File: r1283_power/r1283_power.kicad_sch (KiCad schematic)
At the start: 23 parts, among them J6 Output, J7 Input, U1 R1283K

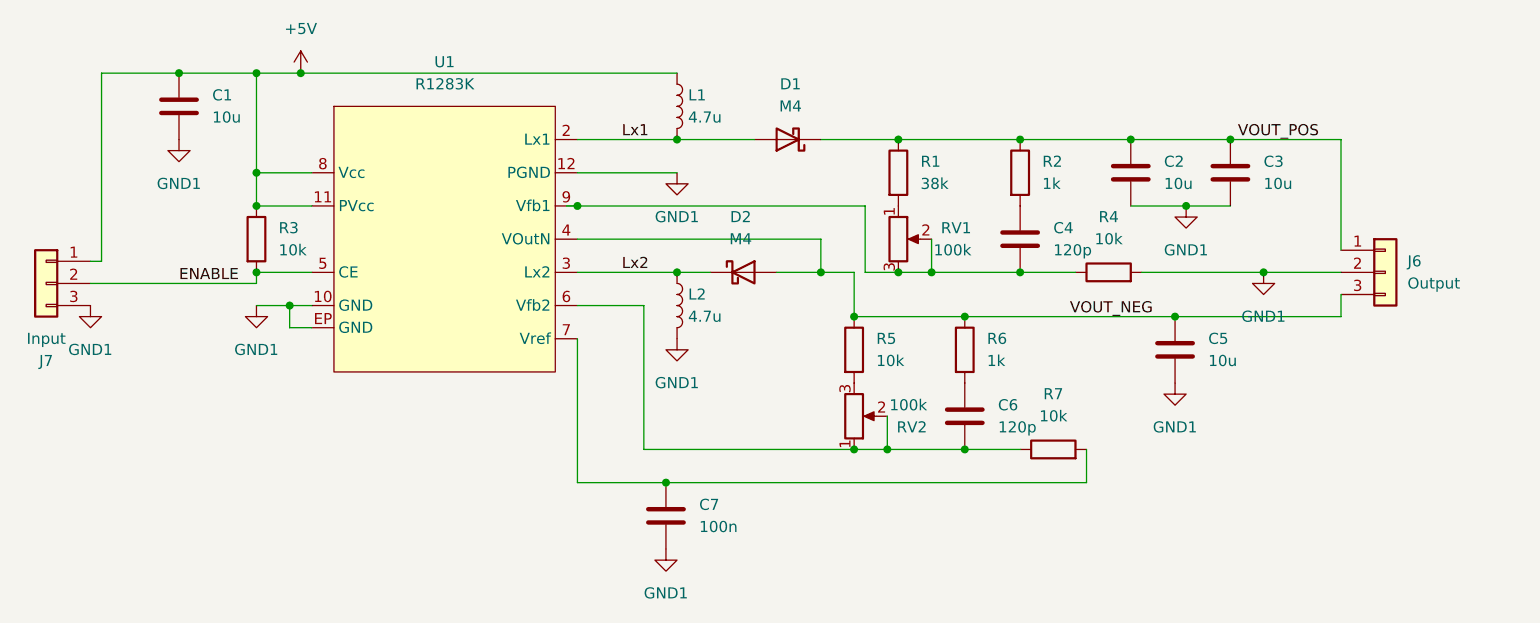
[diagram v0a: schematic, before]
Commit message: added DFN breakout changed trim pot type in 33063_boost, 33063_invert, r1283_power boards fixed error in 33063_boost board (move trim pot to higher side of voltage divider)
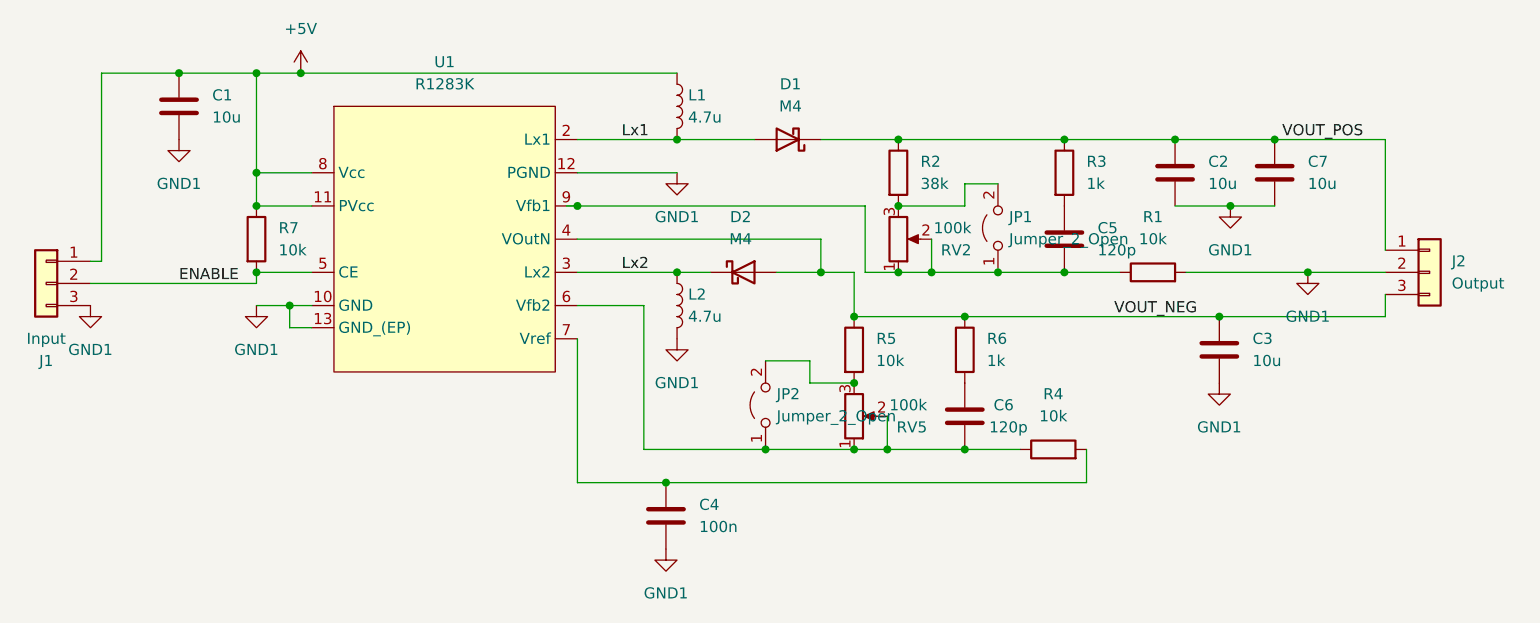
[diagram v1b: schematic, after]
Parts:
- added JP1, JP2: Jumper_2_Open, Jumper:SolderJumper-2_P1.3mm_Open_RoundedPad1.0x1.5mm, symbol Jumper:Jumper_2_Open
- RV2: renamed from RV1; footprint misc:trim_pot -> Potentiometer_THT:Potentiometer_Bourns_3296W_Vertical
- RV5: renamed from RV2; footprint misc:trim_pot -> Potentiometer_THT:Potentiometer_Bourns_3296W_Vertical
- U1: footprint misc:DFN-12-1EP_3x3mm_P0.5mm_EP1.6x2.5mm_hole -> Package_DFN_QFN:DFN-12-1EP_3x3mm_P0.5mm_EP1.6x2.5mm
- renumbered C5 to C3, C7 to C4, C4 to C5, C3 to C7, J7 to J1, J6 to J2, R4 to R1, R1 to R2, R2 to R3, R7 to R4, R3 to R7
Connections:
- net GND1: now also U1.13 (GND_(EP)); no longer U1.EP (GND)
- net at R5.2, RV5.3: now also JP2.2 (B)
- net at C5.2, R1.1, RV2.2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: now also RV2.1, JP1.1 (A); no longer RV2.3
- net at C6.2, R4.1, RV5.1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: now also JP2.1 (A)
- net at R2.2: now also RV2.3, JP1.2 (B); no longer RV2.1
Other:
- moved on the sheet: C2, C3, C5, C7, J2, R1, R3
